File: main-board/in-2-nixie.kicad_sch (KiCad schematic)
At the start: 26 parts, among them J1 Encoder, J2 Matrix, J3 Power, J4 DS3231, J5 Buttons, T1 IN-2, T2 IN-2, T3 IN-2, T4 IN-2, U1 HV5222PJ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

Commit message: pcb
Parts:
- removed C1, C2: 10n, Capacitor_THT:C_Disc_D5.0mm_W2.5mm_P5.00mm, symbol Device:C_Small
- removed J4: DS3231, Connector_PinHeader_2.54mm:PinHeader_1x05_P2.54mm_Vertical, symbol Connector_Generic:Conn_01x05
- removed R7: 10k, Resistor_THT:R_Axial_DIN0207_L6.3mm_D2.5mm_P7.62mm_Horizontal, symbol Device:R_Small
- removed R9: 20k, Resistor_THT:R_Axial_DIN0207_L6.3mm_D2.5mm_P7.62mm_Horizontal, symbol Device:R_Small
- added C1: 330u, Capacitor_THT:CP_Radial_D8.0mm_P3.50mm, symbol Device:C_Polarized
- added D1: 1N4148, Diode_THT:D_DO-35_SOD27_P7.62mm_Horizontal, symbol Diode:1N4148
- added D2, D3, D4, D5: WS2812B, in-2-nixie:APA106_D5-Staggered_Pins, symbol LED:WS2812B
- added J5: BME280, Connector_PinHeader_2.54mm:PinHeader_1x04_P2.54mm_Vertical, symbol Connector_Generic:Conn_01x04
- added J6: DS3231, Connector_PinHeader_2.54mm:PinHeader_1x05_P2.54mm_Vertical, symbol Connector_Generic:Conn_01x05
- added Q1: MPSA42, Package_TO_SOT_THT:TO-92_Inline, symbol Transistor_BJT:MPSA42
- added R10: 33k, Resistor_THT:R_Axial_DIN0207_L6.3mm_D2.5mm_P2.54mm_Vertical, symbol Device:R
- added R6: 10k, Resistor_THT:R_Axial_DIN0207_L6.3mm_D2.5mm_P2.54mm_Vertical, symbol Device:R_Small
- added R9: 200k, Resistor_THT:R_Axial_DIN0207_L6.3mm_D2.5mm_P7.62mm_Horizontal, symbol Device:R
- J1: footprint Connector_PinHeader_2.54mm:PinHeader_1x03_P2.54mm_Vertical -> Connector_PinHeader_2.54mm:PinHeader_1x04_P2.54mm_Vertical; symbol Connector_Generic:Conn_01x03 -> Connector_Generic:Conn_01x04
- J3: renamed from J5; footprint Connector_PinHeader_2.54mm:PinHeader_1x05_P2.54mm_Vertical -> Connector_PinHeader_2.54mm:PinHeader_1x04_P2.54mm_Vertical; symbol Connector_Generic:Conn_01x05 -> Connector_Generic:Conn_01x04
- R1, R2, R4, R5: value R -> 10k
- R3: value R -> 200k
- R8: value 20k -> 10k; footprint Resistor_THT:R_Axial_DIN0207_L6.3mm_D2.5mm_P7.62mm_Horizontal -> Resistor_THT:R_Axial_DIN0207_L6.3mm_D2.5mm_P2.54mm_Vertical
- T1, T2, T3: footprint in-2-nixie:IN-2 Nixie Tube -> in-2-nixie:IN-2 Nixie Tube (w. pins)
- U1: footprint Package_LCC:PLCC-44_16.6x16.6mm_P1.27mm -> in-2-nixie:PLCC-44 LongPads
- renumbered J3 to J4
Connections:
- net +5V: now also C1.1, D1.2 (A), D2.1 (VDD), D3.1 (VDD), D4.1 (VDD), D5.1 (VDD), J5.1 (Pin_1), J6.5 (Pin_5), R6.1; no longer U1.27 (STR), U3.26 (5V)
- net BTN_1: now also J3.4 (Pin_4), U3.4 (GPIO4); no longer J3.5 (Pin_5), U3.3 (GPIO3)
- net BTN_2: now also J3.3 (Pin_3), U3.22 (GPIO22); no longer J3.4 (Pin_4), U3.20 (GPIO20)
- net BTN_3: now also J3.2 (Pin_2), U3.5 (GPIO5); no longer J3.3 (Pin_3), U3.23 (GPIO23)
- net GND: now also R8.1, C1.2, D2.3 (VSS), D3.3 (VSS), D4.3 (VSS), D5.3 (VSS), J5.2 (Pin_2), J6.1 (Pin_1), Q1.1 (E)
- net NIXIE_CLK: now also U4.9 (B3); no longer U4.10 (B2)
- net NIXIE_DIN: now also U4.10 (B2); no longer U4.11 (B1)
- net NIXIE_EN: now also R8.2, U4.8 (B4); no longer U4.9 (B3)
- net ROT_A: now also J1.4 (Pin_4), U3.20 (GPIO20); no longer R8.1, U3.21 (GPIO21)
- net ROT_B: now also J1.3 (Pin_3), U3.14 (GPIO14); no longer U3.22 (GPIO22)
- net SCL: now also J5.3 (Pin_3), J6.3 (Pin_3)
- net SDA: now also J5.4 (Pin_4), J6.4 (Pin_4)
- net ROT_SW: now reaches J1.2 (Pin_2)
- net ROT_SW: now also U3.9 (GPIO9)
- net at R1.2, R2.2, R3.2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: now also R9.2
- net at L2.1 (K): now also L1.1 (K), Q1.3 (C); no longer U1.2 (HVOUT16)
- net at L2.2 (A): now also R9.1; no longer L1.1 (K)
- net at U4.2 (A1): now also U3.3 (GPIO3); no longer U3.0 (GPIO0)
- net at U4.3 (A2): now also U3.2 (GPIO2); no longer U3.1 (GPIO1)
- net at U4.4 (A3): now also U3.1 (GPIO1); no longer U3.2 (GPIO2)
- net at U4.5 (A4): now also U3.0 (GPIO0)
- net LEDS: now reaches U3.8 (GPIO8)
- net LEDS: now also D2.4 (DIN)
- removed net BTN_4: J3.2 (Pin_2), U3.14 (GPIO14)
- new net: D3.2 (DOUT), D4.4 (DIN)
- new net: D2.2 (DOUT), D3.4 (DIN)
- new net: D4.2 (DOUT), D5.4 (DIN)
- new net: Q1.2 (B), R10.2
- new net: D1.1 (K), U3.26 (5V)
- new net: R6.2, U1.27 (STR)
- new net NIXIE_DOT: R10.1, U4.11 (B1)
- no-connect marks 27 -> 23
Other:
- moved on the sheet: C3, J2, J4, L1, L2, R1, R2, R3, R4, R5, T1, T2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

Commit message: update
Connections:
- net GND: now also R8.2; no longer R8.1
- net NIXIE_EN: now also R8.1; no longer R8.2
- net at T1.1 (K1): now also U1.16 (HVOUT2); no longer U1.14 (HVOUT4)
- net at T1.10 (K0): now also U1.17 (HVOUT1); no longer U1.15 (HVOUT3)
- net at T1.2 (K2): now also U1.15 (HVOUT3); no longer U1.13 (HVOUT5)
- net at T1.3 (K3): now also U1.14 (HVOUT4)
- net at T1.4 (K4): now also U1.13 (HVOUT5)
- net at T1.5 (K5): now also U1.12 (HVOUT6)
- net at T2.1 (K1): now also U1.7 (HVOUT11); no longer U1.8 (HVOUT10)
- net at T2.10 (K0): now also U1.11 (HVOUT7); no longer U1.12 (HVOUT6)
- net at T2.2 (K2): now also U1.6 (HVOUT12); no longer U1.7 (HVOUT11)
- net at T2.3 (K3): now also U1.5 (HVOUT13); no longer U1.6 (HVOUT12)
- net at T2.4 (K4): now also U1.4 (HVOUT14); no longer U1.5 (HVOUT13)
- net at T2.5 (K5): now also U1.3 (HVOUT15); no longer U1.4 (HVOUT14)
- net at T2.6 (K6): now also U1.2 (HVOUT16); no longer U1.3 (HVOUT15)
- net at T2.7 (K7): now also U1.8 (HVOUT10); no longer U1.9 (HVOUT9)
- net at T2.8 (K8): now also U1.9 (HVOUT9); no longer U1.10 (HVOUT8)
- net at T2.9 (K9): now also U1.10 (HVOUT8); no longer U1.11 (HVOUT7)
- no-connect marks 23 -> 17

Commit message: pcb final
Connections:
- net +3.3V: now also J2.1 (Pin_1), J5.1 (Pin_1), J6.5 (Pin_5)
- net +5V: no longer J2.1 (Pin_1), J5.1 (Pin_1), J6.5 (Pin_5)
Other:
- moved on the sheet: C1, C3, D1, D2, D3, D4, D5, J1, J2, J3, J4, J5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

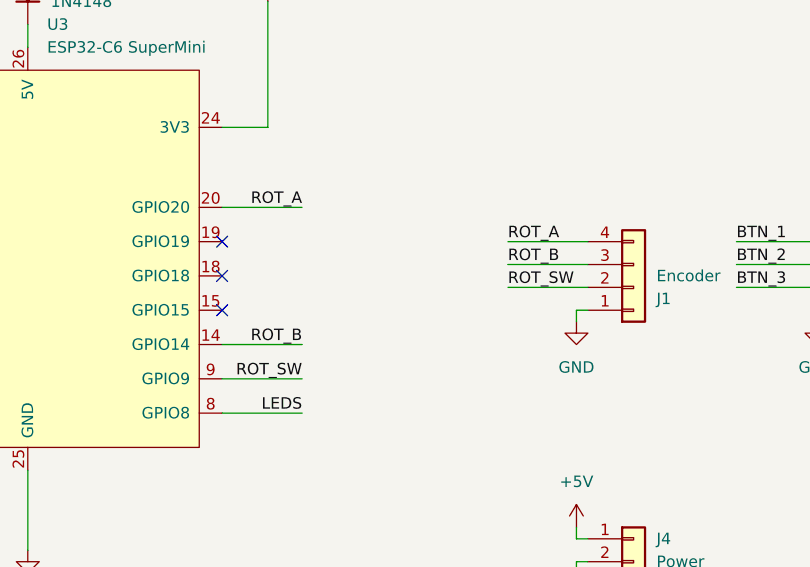
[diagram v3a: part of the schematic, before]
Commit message: fix encoder routing
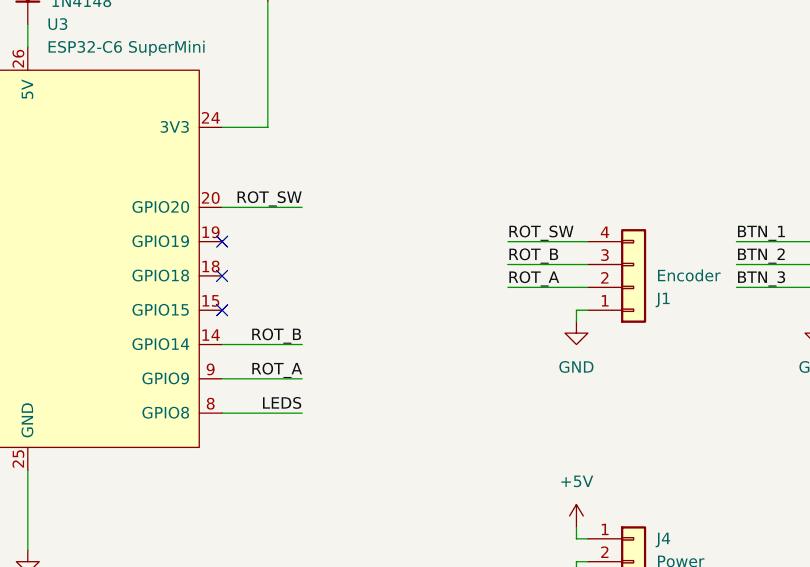
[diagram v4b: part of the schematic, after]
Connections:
- net ROT_A: now also J1.2 (Pin_2), U3.9 (GPIO9); no longer J1.4 (Pin_4), U3.20 (GPIO20)
- net ROT_SW: now also J1.4 (Pin_4), U3.20 (GPIO20); no longer J1.2 (Pin_2), U3.9 (GPIO9)
